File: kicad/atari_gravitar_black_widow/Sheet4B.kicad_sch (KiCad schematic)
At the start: 45 parts

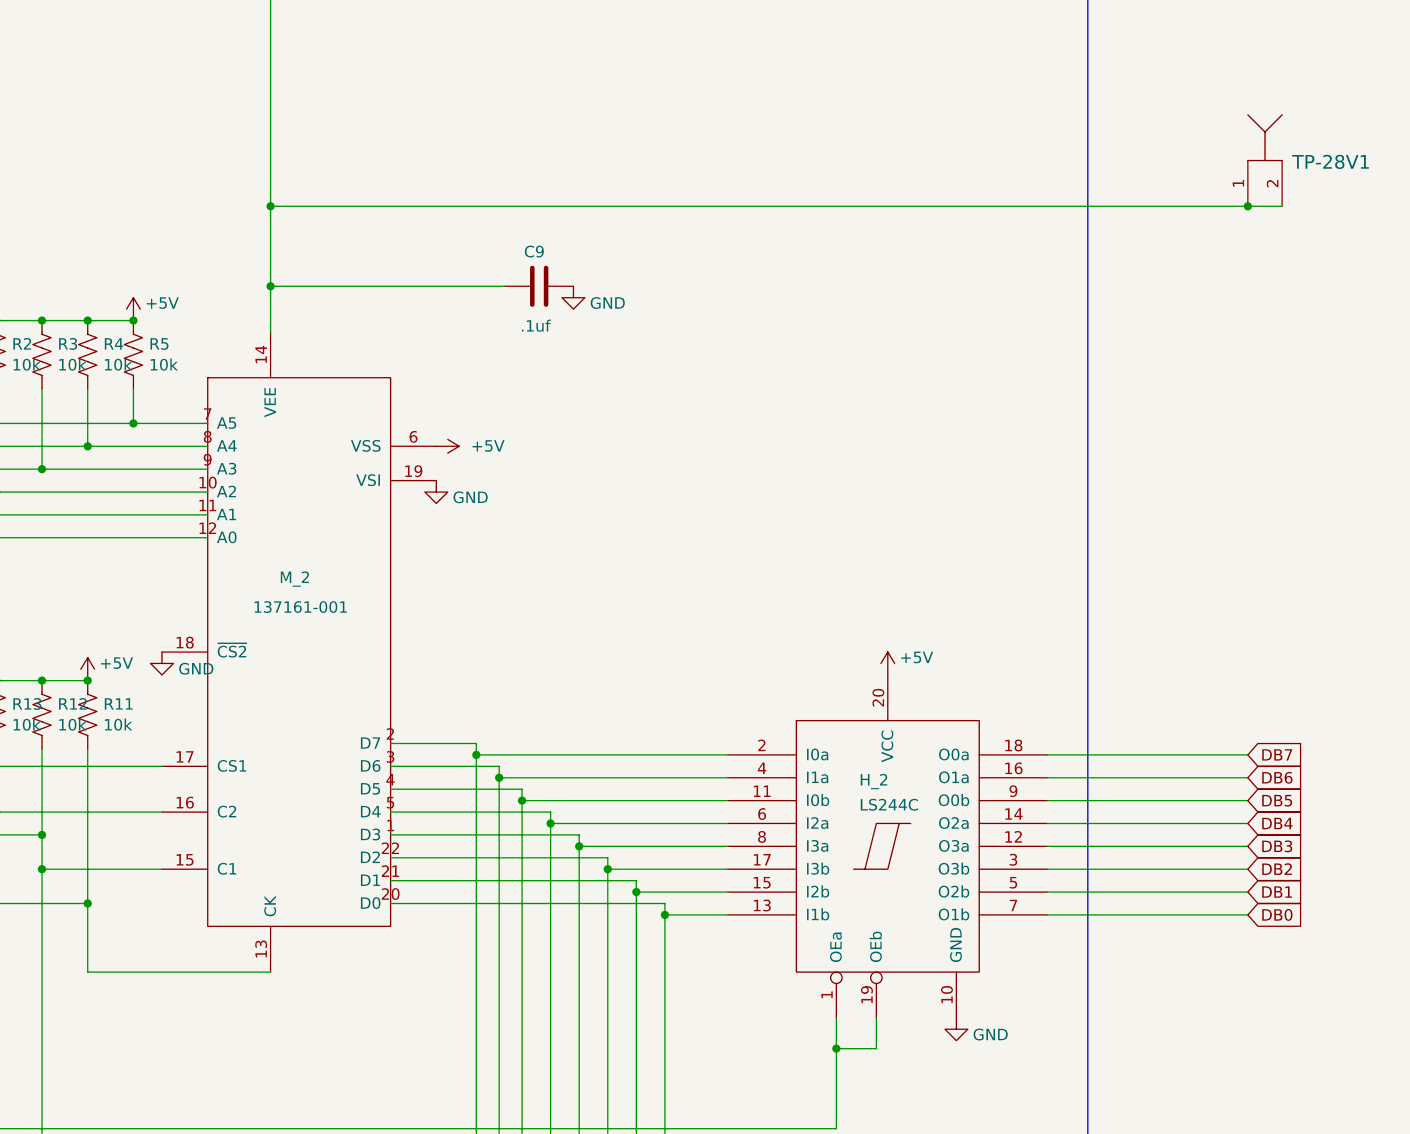
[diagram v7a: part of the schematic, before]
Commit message: Fixed all schematic warnings and fixed the edge cuts
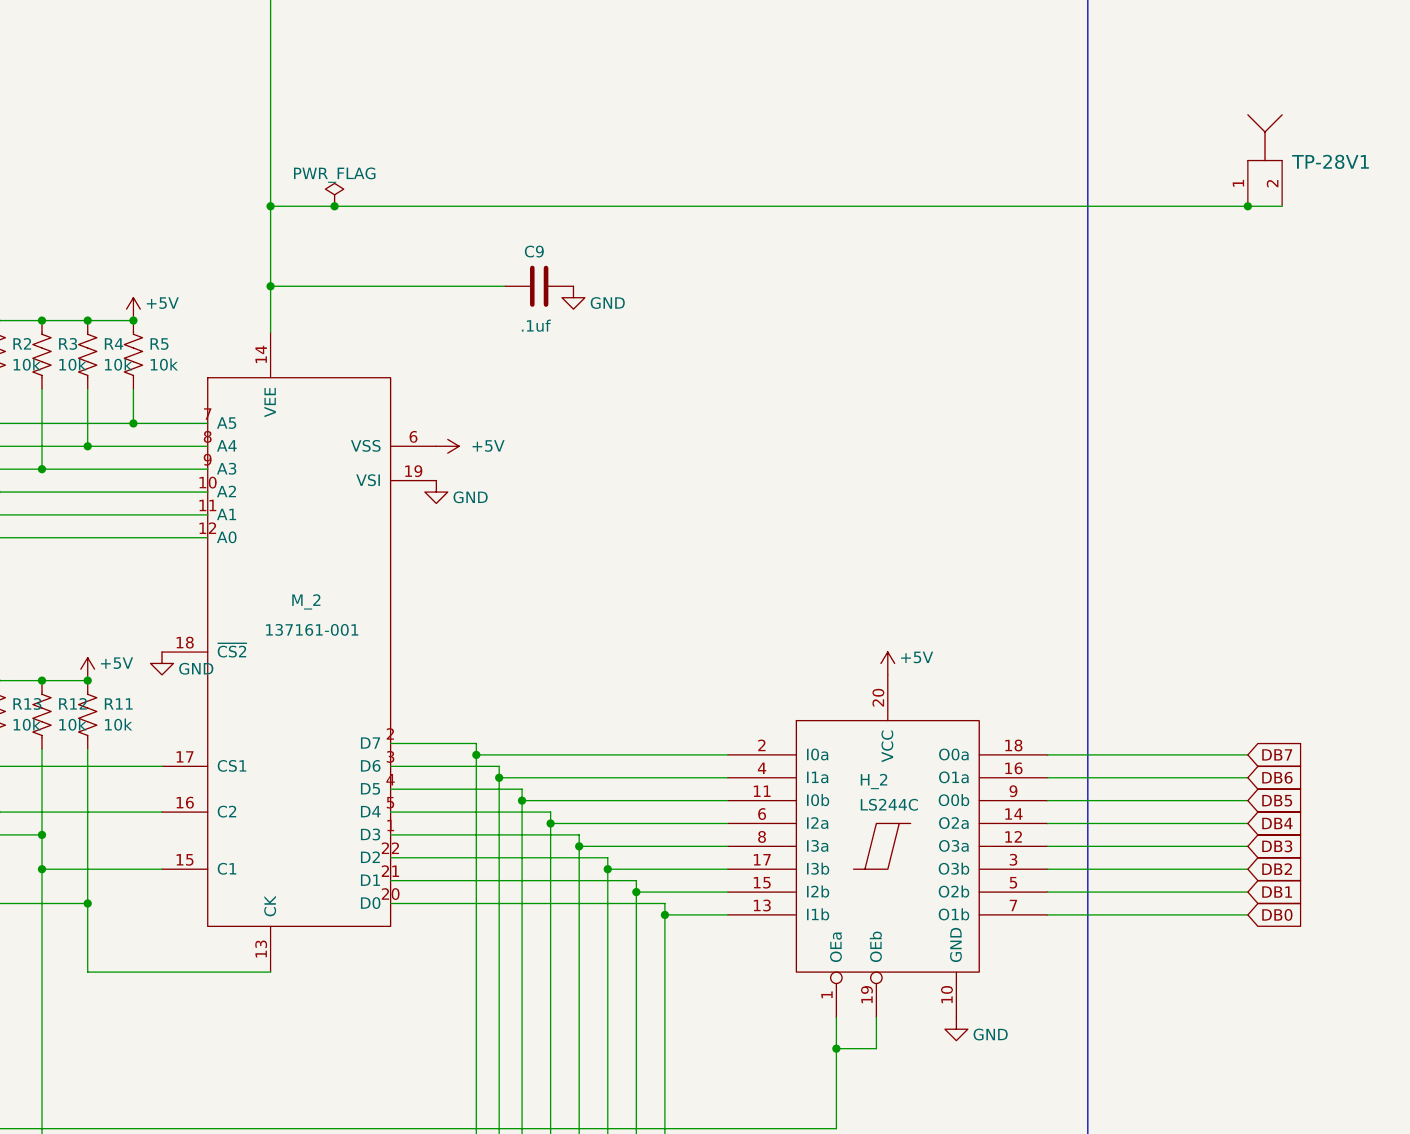
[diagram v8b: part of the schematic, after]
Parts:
- M_2: footprint Package_DIP:DIP-22_W10.16mm -> Gravitar:EAROM
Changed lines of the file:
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@@
   (junction (at 121.285 106.68) (diameter 0) (color 0 0 0 0)
+  )
+  (junction (at 445.262 127) (diameter 0) (color 0 0 0 0)
   )
   (junction (at 156.845 72.39) (diameter 0) (color 0 0 0 0)
@@
     (stroke (width 0) (type default) (color 0 0 0 0))
   )
-  (wire (pts (xy 438.15 127) (xy 546.735 127))
+  (wire (pts (xy 438.15 127) (xy 445.262 127))
     (stroke (width 0) (type default) (color 0 0 0 0))
   )
@@
   )
   (wire (pts (xy 451.485 196.85) (xy 472.44 196.85))
+    (stroke (width 0) (type default) (color 0 0 0 0))
+  )
+  (wire (pts (xy 445.262 127) (xy 546.735 127))
     (stroke (width 0) (type default) (color 0 0 0 0))
   )
@@
       (effects (font (size 1.27 1.27)) (justify right) hide)
     )
+  )
+  (symbol (lib_id "power:PWR_FLAG") (at 445.262 127 0) (unit 1)
+    (in_bom yes) (on_board yes) (fields_autoplaced)
+    (property "Reference" "#FLG0108" (id 0) (at 445.262 125.095 0)
+      (effects (font (size 1.27 1.27)) hide)
+    )
+    (property "Value" "PWR_FLAG" (id 1) (at 445.262 123.3955 0))
+    (property "Footprint" "" (id 2) (at 445.262 127 0)
+      (effects (font (size 1.27 1.27)) hide)
+    )
+    (property "Datasheet" "~" (id 3) (at 445.262 127 0)
+      (effects (font (size 1.27 1.27)) hide)
+    )
+    (pin "1")
   )
   (symbol (lib_id "Device:R_US") (at 487.045 255.905 270) (unit 1)
@@
     (pin "1")
   )
-  (symbol (lib_id "atari_grav_bw:137161") (at 441.325 173.99 0) (unit 1)
+  (symbol (lib_id "atari_grav_bw:137161") (at 442.595 176.53 0) (unit 1)
     (in_bom yes) (on_board yes)
-    (property "Reference" "M_2" (id 0) (at 442.595 168.275 0)
+    (property "Reference" "M_2" (id 0) (at 443.865 170.815 0)
       (effects (font (size 1.27 1.27)) (justify right))
     )
-    (property "Value" "137161-001" (id 1) (at 446.786 171.577 0)
+    (property "Value" "137161-001" (id 1) (at 448.056 174.117 0)
       (effects (font (size 1.27 1.27)) (justify right))
     )
-    (property "Footprint" "Package_DIP:DIP-22_W10.16mm" (id 2) (at 441.325 167.64 0)
-      (effects (font (size 1.27 1.27)) hide)
-    )
-    (property "Datasheet" "" (id 3) (at 441.325 167.64 0)
-      (effects (font (size 1.27 1.27)) hide)
-    )
+    (property "Footprint" "Gravitar:EAROM" (id 2) (at 442.595 170.18 0)
+      (effects (font (size 1.27 1.27)) hide)
+    )
+    (property "Datasheet" "" (id 3) (at 442.595 170.18 0)
+      (effects (font (size 1.27 1.27)) hide)
+    )
